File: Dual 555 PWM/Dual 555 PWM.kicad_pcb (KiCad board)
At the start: 2 copper layers, 13 parts, among them J1 Conn_01x04_Male, U1 TLC555, U2 TLC555

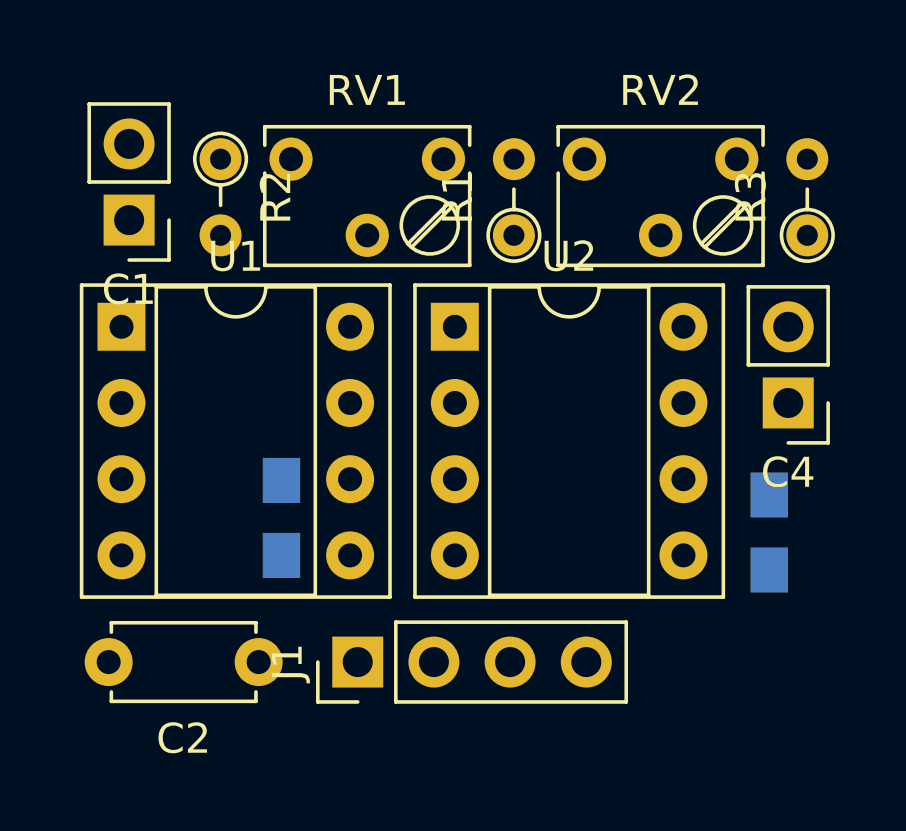
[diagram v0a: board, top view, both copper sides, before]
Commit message: Silk screen edits
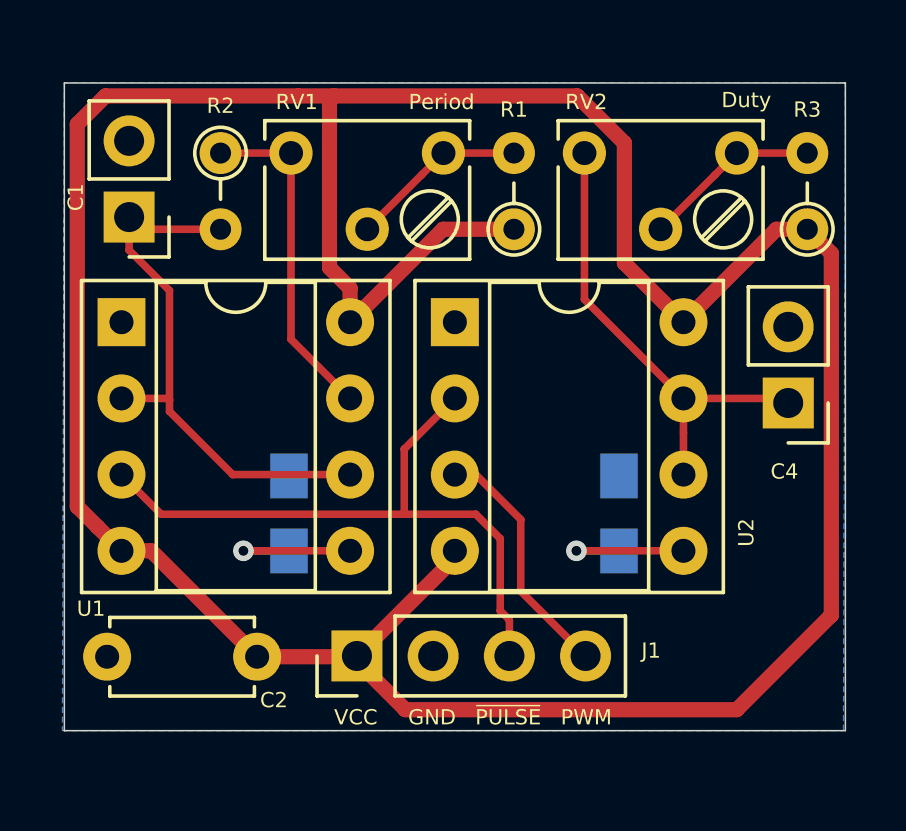
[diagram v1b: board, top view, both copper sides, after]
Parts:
- moved C5 5.04 mm to (85.2, 72.8)
- moved C3 0.29 mm to (74.2, 72.8)
- moved J1 0.20 mm to (76.4, 77.5)
- moved R1 0.20 mm to (81.7, 63.3)
- moved R2 0.20 mm to (71.9, 60.8)
- moved R3 0.20 mm to (91.4, 63.3)
- moved RV1 0.20 mm to (79.3, 60.8)
- moved RV2 0.20 mm to (89.1, 60.8)
- moved C2 0.18 mm to (73.1, 77.5)
- moved U1 0.15 mm to (68.6, 66.4)
- moved U2 0.15 mm to (79.7, 66.4)
- moved C1 0.10 mm to (68.8, 62.9)
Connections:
- net VCC renamed Net-(C2-Pad1)
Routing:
- net Net-(C2-Pad1): track 0.00 -> 106.3 mm
- net /~PULSE: track 0.00 -> 22.1 mm
- net Net-(C1-Pad1): track 0.00 -> 18.8 mm
- net Net-(C4-Pad1): track 0.00 -> 15.6 mm
- net Net-(R2-Pad1): track 0.00 -> 11.3 mm
- net /PWM: track 0.00 -> 8.26 mm
- net Net-(R1-Pad2): track 0.00 -> 5.94 mm
- net Net-(R3-Pad2): track 0.00 -> 5.94 mm
- net Net-(C3-Pad1): track 0.00 -> 5.08 mm, vias 0 -> 1
- net Net-(C5-Pad1): track 0.00 -> 4.99 mm, vias 0 -> 1
- added copper zone on B.Cu, net GND
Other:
- board outline added: 26 x 21.6 mm
- net class Default: clearance 0.2 -> 0.1524; trace_width 0.25 -> 0.1524; via_dia 0.8 -> 0.6858; via_drill 0.4 -> 0.3302
- net class VCC added: clearance 0.254, trace_width 0.508, via_dia 0.762, via_drill 0.381
- rule pad_to_mask_clearance: 0.051 -> 0.0508
- rule solder_mask_min_width: 0.25 -> 0.1016
- rule trace_clearance: 0.2 -> 0.1524
- rule trace_min: 0.2 -> 0.1524
- rule via_min_drill: 0.3 -> 0.254
- rule via_min_size: 0.4 -> 0.508
- board text added: "Dual 555 PWM Rev A 2021 Bobrowicz P."
- board text added: "Duty"
- board text added: "GND"
- board text added: "PWM"
- board text added: "Period"
- board text added: "VCC"
- board text added: "~PULSE"
